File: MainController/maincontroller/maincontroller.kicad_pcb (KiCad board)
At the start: 2 copper layers, 30 parts, among them J1 LED, J2 Receiver, J3 5VIN, J4 Analog_Motor, J5 OneWire, J6 Conn_01x04, SW1 SW_Push

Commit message: main controller pcb
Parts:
- added J7: Conn_01x02, Connector_JST:JST_EH_B02B-EH-A_1x02_P2.50mm_Vertical, F.Cu at (102.9, 45.7)
- added J8: Conn_01x05_Female, Connector_JST:JST_EH_B05B-EH-A_1x05_P2.50mm_Vertical, F.Cu at (109.2, 55.9)
- J6: value Conn_01x04 -> Hall_In
- R11, R14: footprint Resistor_THT:R_Axial_DIN0309_L9.0mm_D3.2mm_P12.70mm_Horizontal -> Resistor_THT:R_Axial_DIN0207_L6.3mm_D2.5mm_P2.54mm_Vertical
- R12, R13: footprint Resistor_THT:R_Axial_DIN0309_L9.0mm_D3.2mm_P12.70mm_Horizontal -> Resistor_THT:R_Axial_DIN0309_L9.0mm_D3.2mm_P2.54mm_Vertical
- R15: footprint Resistor_THT:R_Axial_DIN0204_L3.6mm_D1.6mm_P2.54mm_Vertical -> Resistor_THT:R_Axial_DIN0207_L6.3mm_D2.5mm_P7.62mm_Horizontal
- R16, R17, R18: footprint Resistor_THT:R_Axial_DIN0204_L3.6mm_D1.6mm_P2.54mm_Vertical -> Resistor_THT:R_Axial_DIN0309_L9.0mm_D3.2mm_P12.70mm_Horizontal
- R5: footprint Resistor_THT:R_Axial_DIN0204_L3.6mm_D1.6mm_P2.54mm_Vertical -> Resistor_THT:R_Axial_DIN0411_L9.9mm_D3.6mm_P12.70mm_Horizontal
- SW1: footprint Button_Switch_SMD:SW_SPST_B3S-1000 -> Button_Switch_THT:SW_DIP_SPSTx01_Piano_10.8x4.1mm_W7.62mm_P2.54mm
- moved J5 121.8 mm to (91.4, 59.7), turned to 90 degrees
- moved R8 88.7 mm to (158.6, 60.3), turned to 90 degrees
- moved R14 88.3 mm to (166.4, 58.4), turned to 270 degrees
- moved R10 87.8 mm to (163.7, 60.3), turned to 90 degrees
- moved R12 87.4 mm to (171.4, 58.4), turned to 270 degrees
- moved R5 86.3 mm to (101.6, 77.5), turned to 90 degrees
- moved R7 82.8 mm to (156.0, 60.3), turned to 90 degrees
- moved R15 82.4 mm to (172.7, 78.1), turned to 90 degrees
- moved R11 81.8 mm to (174.0, 58.4), turned to 270 degrees
- moved R6 80.8 mm to (96.5, 77.5), turned to 90 degrees
- moved R9 79.5 mm to (161.1, 60.3), turned to 90 degrees
- moved R13 79.5 mm to (168.9, 58.4), turned to 270 degrees
- moved R17 76.1 mm to (161.3, 76.2), turned to 90 degrees
- moved J1 76.0 mm to (91.4, 74.9), turned to 90 degrees
- moved R2 74.0 mm to (132.1, 81.3), turned to 90 degrees
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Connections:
- J2 pad 5: Net-(Hinten_links1-Pad2) -> Net-(Hinten_links1-Pad1)
- J2 pad 6: Net-(Hinten_links1-Pad1) -> Net-(Hinten_links1-Pad2)
- J3 pad 2: Net-(Hinten_links1-Pad1) -> Net-(Hinten_links1-Pad2)
- J3 pad 3: Net-(Hinten_links1-Pad2) -> Net-(Hinten_links1-Pad1)
- XA1 pad A6: Net-(R15-Pad1) -> Net-(R17-Pad1)
- XA1 pad A7: Net-(R16-Pad1) -> Net-(R18-Pad1)
- XA1 pad A8: Net-(R17-Pad1) -> Net-(R16-Pad1)
- XA1 pad A9: Net-(R18-Pad1) -> Net-(R15-Pad1)
- XA1 pad D50: Net-(J2-Pad1) -> Net-(J2-Pad2)
- XA1 pad D51: Net-(J2-Pad2) -> Net-(J2-Pad3)
- XA1 pad D52: Net-(J2-Pad3) -> Net-(J2-Pad1)
- XA1 pad GND: Net-(Hinten_links1-Pad1) -> (no net)
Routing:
- net Net-(Hinten_links1-Pad1): track 0.00 -> 267.6 mm
- net Net-(Hinten_links1-Pad2): track 0.00 -> 149.5 mm
- net Net-(J5-Pad1): track 0.00 -> 86.1 mm
- net Net-(R5-Pad1): track 0.00 -> 46.0 mm
- net Net-(J1-Pad2): track 0.00 -> 45.3 mm
- net Net-(J1-Pad3): track 0.00 -> 38.7 mm
- net Net-(J4-Pad4): track 0.00 -> 34.7 mm
- net Net-(R11-Pad2): track 0.00 -> 33.8 mm
- net Net-(Vorne_links1-Pad3): track 0.00 -> 31.8 mm
- net Net-(Hinten_rechts1-Pad3): track 0.00 -> 30.2 mm
- net Net-(Vorne_rechts1-Pad3): track 0.00 -> 29.7 mm
- net Net-(Vorne_links1-Pad4): track 0.00 -> 28.3 mm
- net Net-(Hinten_links1-Pad3): track 0.00 -> 27.6 mm
- net Net-(R18-Pad1): track 0.00 -> 27.0 mm
- net Net-(R17-Pad1): track 0.00 -> 26.5 mm
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- added copper zone on B.Cu, net Net-(Hinten_links1-Pad1)
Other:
- board outline added: 99.1 x 62.2 mm
- net class Default: clearance 1 -> 0.3; trace_width 1 -> 0.8
- net class small added: clearance 0.5, trace_width 0.8, via_dia 0.8, via_drill 0.4
- rule trace_clearance: 1 -> 0.3

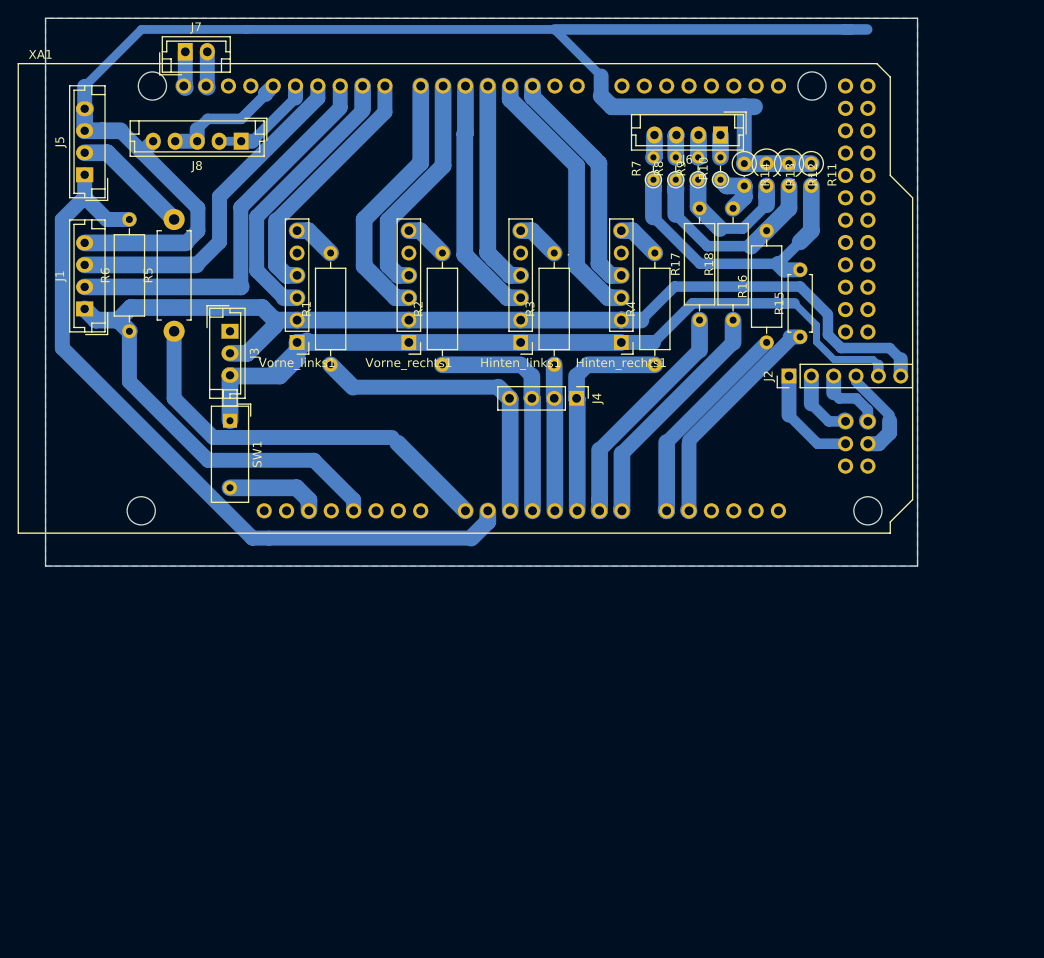
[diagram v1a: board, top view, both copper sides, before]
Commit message: removed 5v in, use reciver power instead, simplified relay connector, added reverse pin to motorconnector
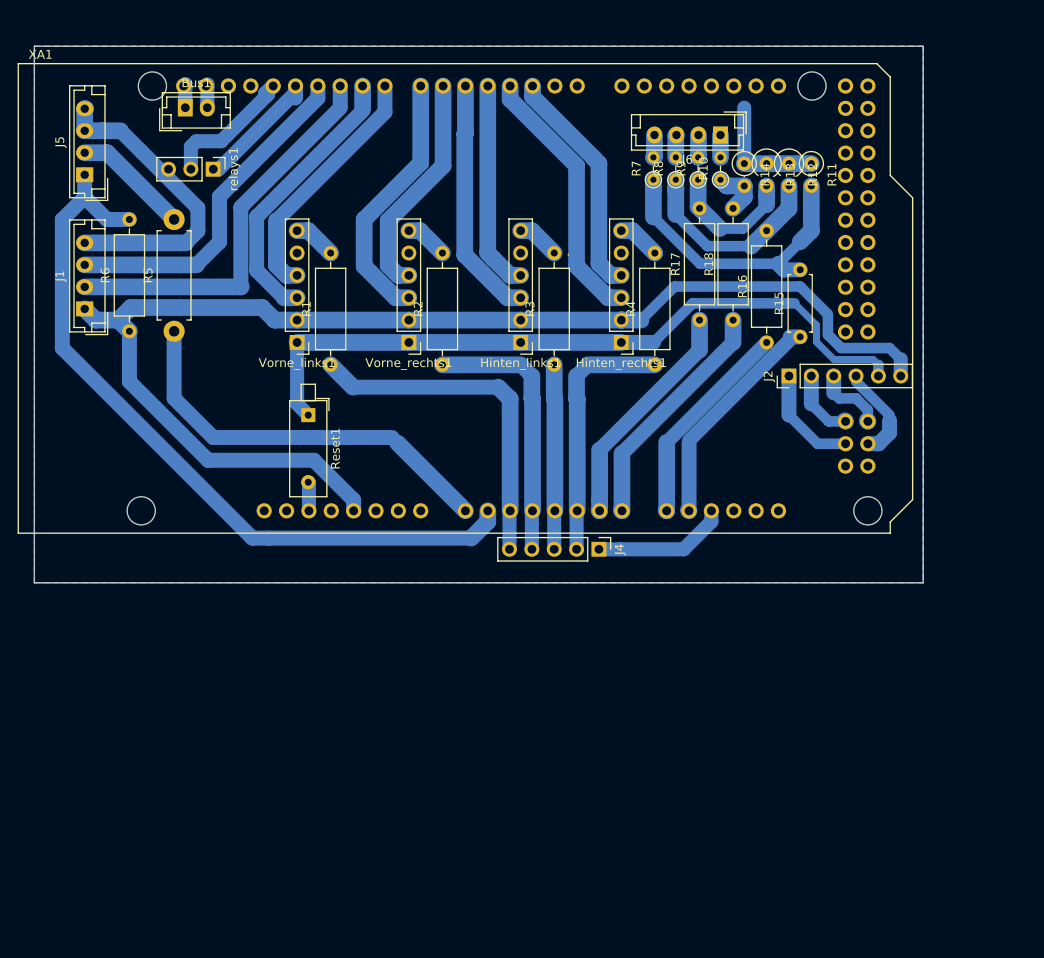
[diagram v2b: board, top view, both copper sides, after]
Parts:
- removed J3: 5VIN, Connector_JST:JST_EH_B03B-EH-A_1x03_P2.50mm_Vertical
- removed J7: Conn_01x02, Connector_JST:JST_EH_B02B-EH-A_1x02_P2.50mm_Vertical
- removed J8: Conn_01x05_Female, Connector_JST:JST_EH_B05B-EH-A_1x05_P2.50mm_Vertical
- removed SW1: SW_Push, Button_Switch_THT:SW_DIP_SPSTx01_Piano_10.8x4.1mm_W7.62mm_P2.54mm
- added Bus1: Conn_01x02, Connector_JST:JST_EH_B02B-EH-A_1x02_P2.50mm_Vertical, F.Cu at (102.9, 52.1)
- added Reset1: SW_Push, Button_Switch_THT:SW_DIP_SPSTx01_Piano_10.8x4.1mm_W7.62mm_P2.54mm, F.Cu at (116.8, 87.0)
- added relays1: Conn_01x05_Female, Connector_PinHeader_2.54mm:PinHeader_1x03_P2.54mm_Vertical, F.Cu at (106.0, 59.1)
- J4: footprint Connector_PinHeader_2.54mm:PinHeader_1x04_P2.54mm_Vertical -> Connector_PinHeader_2.54mm:PinHeader_1x05_P2.54mm_Vertical
- moved J4 17.3 mm to (149.9, 102.2)
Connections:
- R1 pad 1: Net-(J4-Pad4) -> Net-(J4-Pad5)
- R2 pad 1: Net-(J4-Pad3) -> Net-(J4-Pad4)
- R3 pad 1: Net-(J4-Pad2) -> Net-(J4-Pad3)
- R4 pad 1: Net-(J4-Pad1) -> Net-(J4-Pad2)
- XA1 pad A10: Net-(XA1-PadA10) -> Net-(J4-Pad1)
- XA1 pad A2: Net-(J4-Pad4) -> Net-(J4-Pad5)
- XA1 pad A3: Net-(J4-Pad3) -> Net-(J4-Pad4)
- XA1 pad A4: Net-(J4-Pad2) -> Net-(J4-Pad3)
- XA1 pad A5: Net-(J4-Pad1) -> Net-(J4-Pad2)
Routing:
- net Net-(Hinten_links1-Pad1): track 267.6 -> 131.1 mm
- net Net-(J4-Pad5): track 0.00 -> 39.1 mm
- net Net-(J4-Pad2): track 16.6 -> 29.2 mm
- net Net-(J4-Pad1): track 24.8 -> 15.3 mm
- net Net-(Reset1-Pad2): track 10.8 -> 3.28 mm
- net Net-(Hinten_links1-Pad2): track 149.5 -> 142.5 mm
- net Net-(J4-Pad3): track 26.0 -> 21.0 mm
- net Net-(J4-Pad4): track 34.7 -> 30.4 mm
- net Net-(XA1-PadD12): track 12.1 -> 15.1 mm
- net Net-(XA1-PadD13): track 14.8 -> 16.3 mm
- net Net-(Bus1-Pad2): track 4.14 -> 2.72 mm
- net Net-(Bus1-Pad1): track 4.21 -> 2.79 mm
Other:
- board size 99.1 x 62.2 mm -> 101 x 61 mm
- net class Default: trace_width 0.8 -> 1.6

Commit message: main rework
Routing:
- net Net-(XA1-PadD13): track 16.3 -> 2.51 mm
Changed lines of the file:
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@@
-(kicad_pcb (version 20171130) (host pcbnew "(5.0.0)")
+(kicad_pcb (version 20171130) (host pcbnew 5.0.0)
   (general
     (thickness 1.6)
     (drawings 1)
-    (tracks 256)
+    (tracks 252)
     (zones 0)
     (modules 31)
@@
     (42 Eco1.User user)
     (43 Eco2.User user)
-    (44 Edge.Cuts user)
+    (44 Edge.Cuts user hide)
     (45 Margin user)
     (46 B.CrtYd user)
@@
   (segment (start 112.851001 49.605001) (end 111.987402 50.4686) (width 1.7) (layer B.Cu) (net 87))
   (segment (start 111.987402 50.4686) (end 111.987402 50.572598) (width 1.7) (layer B.Cu) (net 87))
-  (segment (start 103.505 56.515) (end 103.505 59.055) (width 1.6) (layer B.Cu) (net 87))
-  (segment (start 104.14 55.88) (end 103.505 56.515) (width 1.6) (layer B.Cu) (net 87))
-  (segment (start 106.942132 55.88) (end 104.14 55.88) (width 1.6) (layer B.Cu) (net 87))
-  (segment (start 112.274602 50.54753) (end 106.942132 55.88) (width 1.6) (layer B.Cu) (net 87))
   (segment (start 112.851001 49.605001) (end 112.274602 50.1814) (width 1.6) (layer B.Cu) (net 87))
   (segment (start 112.274602 50.1814) (end 112.274602 50.54753) (width 1.6) (layer B.Cu) (net 87))
